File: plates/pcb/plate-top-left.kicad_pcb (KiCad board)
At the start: 2 copper layers, 125.1 x 92.6 mm, 0 parts

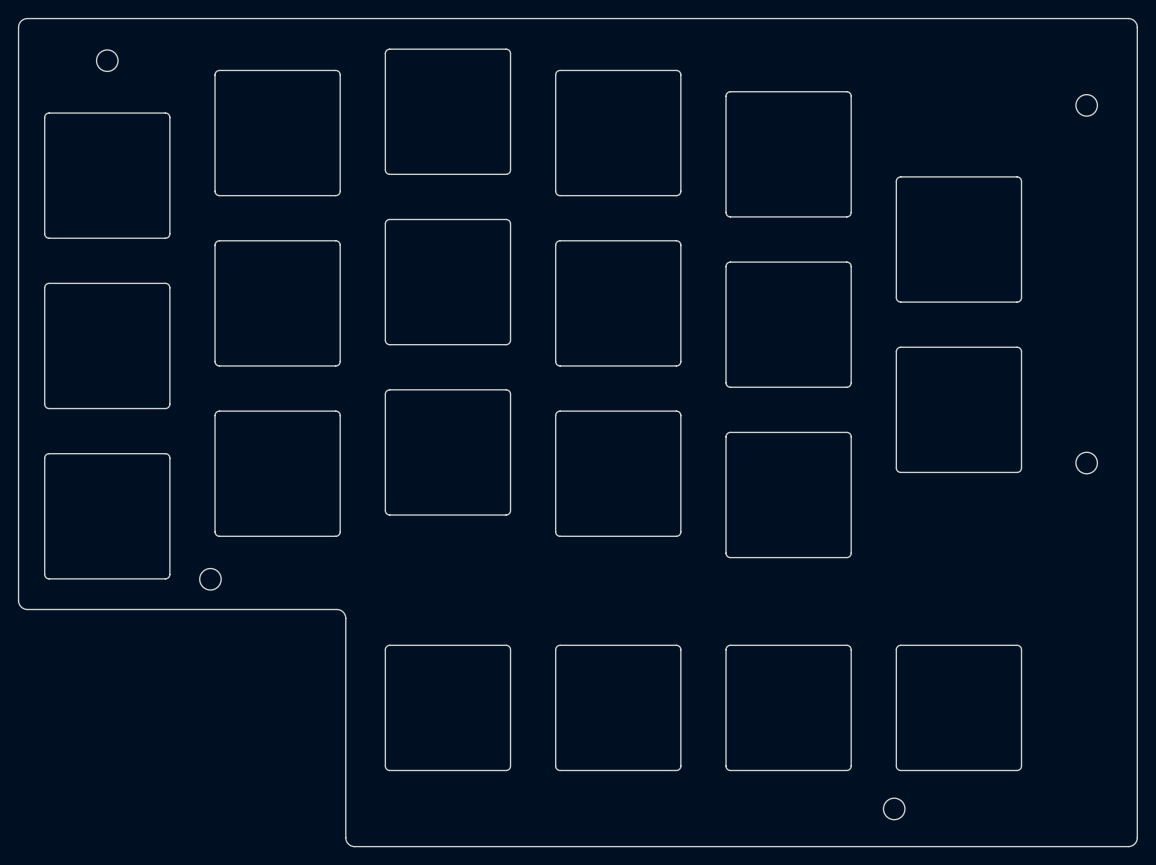
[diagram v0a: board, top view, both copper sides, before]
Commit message: fix(cad): update Z-stackup, 6mm cup standoffs, cup ear/plate clearances, ceramic ball throat, and sensor/CKW12 models
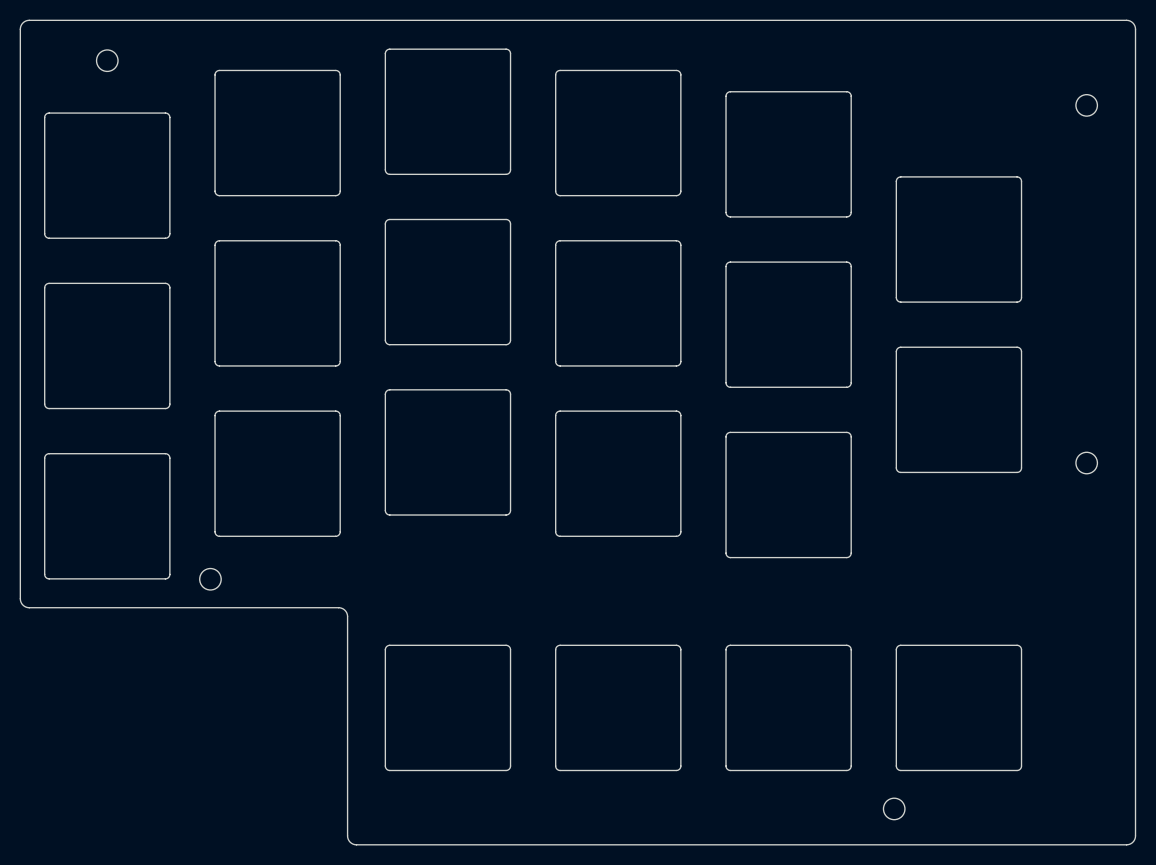
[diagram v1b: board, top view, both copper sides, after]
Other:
- board size 125.1 x 92.6 mm -> 124.7 x 92.2 mm
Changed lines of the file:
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@@
 	)
 	(gr_line
-		(start -119.4625 -23.7125)
-		(end -119.4625 40.38125)
-		(stroke
-			(width 0.15)
-			(type default)
-		)
-		(layer "Edge.Cuts")
-	)
-	(gr_arc
-		(start -119.4625 -23.7125)
-		(mid -119.169607 -24.419607)
-		(end -118.4625 -24.7125)
-		(stroke
-			(width 0.15)
-			(type default)
-		)
-		(layer "Edge.Cuts")
-	)
-	(gr_arc
-		(start -118.4625 41.38125)
-		(mid -119.169607 41.088357)
-		(end -119.4625 40.38125)
-		(stroke
-			(width 0.15)
-			(type default)
-		)
-		(layer "Edge.Cuts")
-	)
-	(gr_line
-		(start -118.4625 41.38125)
-		(end -83.8625 41.38125)
+		(start -119.2625 -23.5125)
+		(end -119.2625 40.18125)
+		(stroke
+			(width 0.15)
+			(type default)
+		)
+		(layer "Edge.Cuts")
+	)
+	(gr_arc
+		(start -119.2625 -23.5125)
+		(mid -118.969607 -24.219607)
+		(end -118.2625 -24.5125)
+		(stroke
+			(width 0.15)
+			(type default)
+		)
+		(layer "Edge.Cuts")
+	)
+	(gr_arc
+		(start -118.2625 41.18125)
+		(mid -118.969607 40.888357)
+		(end -119.2625 40.18125)
+		(stroke
+			(width 0.15)
+			(type default)
+		)
+		(layer "Edge.Cuts")
+	)
+	(gr_line
+		(start -118.2625 41.18125)
+		(end -83.6625 41.18125)
 		(stroke
 			(width 0.15)
@@
 	)
 	(gr_arc
-		(start -83.8625 41.38125)
-		(mid -83.155393 41.674143)
-		(end -82.8625 42.38125)
+		(start -83.6625 41.18125)
+		(mid -82.955393 41.474143)
+		(end -82.6625 42.18125)
 		(stroke
 			(width 0.15)
@@
 	)
 	(gr_line
-		(start -82.8625 42.38125)
-		(end -82.8625 66.9)
-		(stroke
-			(width 0.15)
-			(type default)
-		)
-		(layer "Edge.Cuts")
-	)
-	(gr_arc
-		(start -81.8625 67.9)
-		(mid -82.569607 67.607107)
-		(end -82.8625 66.9)
-		(stroke
-			(width 0.15)
-			(type default)
-		)
-		(layer "Edge.Cuts")
-	)
-	(gr_line
-		(start -81.8625 67.9)
-		(end 4.6625 67.9)
+		(start -82.6625 42.18125)
+		(end -82.6625 66.7)
+		(stroke
+			(width 0.15)
+			(type default)
+		)
+		(layer "Edge.Cuts")
+	)
+	(gr_arc
+		(start -81.6625 67.7)
+		(mid -82.369607 67.407107)
+		(end -82.6625 66.7)
+		(stroke
+			(width 0.15)
+			(type default)
+		)
+		(layer "Edge.Cuts")
+	)
+	(gr_line
+		(start -81.6625 67.7)
+		(end 4.4625 67.7)
 		(stroke
 			(width 0.15)
@@
 	)
 	(gr_line
-		(start 4.6625 -24.7125)
-		(end -118.4625 -24.7125)
-		(stroke
-			(width 0.15)
-			(type default)
-		)
-		(layer "Edge.Cuts")
-	)
-	(gr_arc
-		(start 4.6625 -24.7125)
-		(mid 5.369607 -24.419607)
-		(end 5.6625 -23.7125)
-		(stroke
-			(width 0.15)
-			(type default)
-		)
-		(layer "Edge.Cuts")
-	)
-	(gr_arc
-		(start 5.6625 66.9)
-		(mid 5.369607 67.607107)
-		(end 4.6625 67.9)
-		(stroke
-			(width 0.15)
-			(type default)
-		)
-		(layer "Edge.Cuts")
-	)
-	(gr_line
-		(start 5.6625 66.9)
-		(end 5.6625 -23.7125)
-		(stroke
-			(width 0.15)
+		(start 4.4625 -24.5125)
+		(end -118.2625 -24.5125)
+		(stroke
+			(width 0.15)
+			(type default)
+		)
+		(layer "Edge.Cuts")
+	)
+	(gr_arc
+		(start 4.4625 -24.5125)
+		(mid 5.169607 -24.219607)
+		(end 5.4625 -23.5125)
+		(stroke
+			(width 0.15)
+			(type default)
+		)
+		(layer "Edge.Cuts")
+	)
+	(gr_arc
+		(start 5.4625 66.7)
+		(mid 5.169607 67.407107)
+		(end 4.4625 67.7)
+		(stroke
+			(width 0.15)
+			(type default)
+		)
+		(layer "Edge.Cuts")
+	)
+	(gr_line
+		(start 5.4625 66.7)
+		(end 5.4625 -23.5125)
+		(stroke
+			(width 0.15)

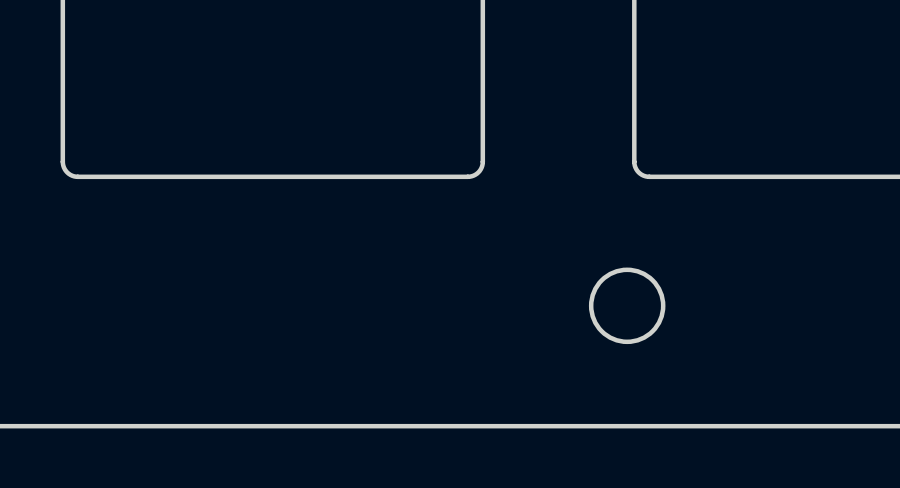
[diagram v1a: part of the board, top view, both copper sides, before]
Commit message: feat(pcb): separate pmw3360 sensor PCB with JST SH 6-pin connector and add symmetric thumb mounting holes L5/R5
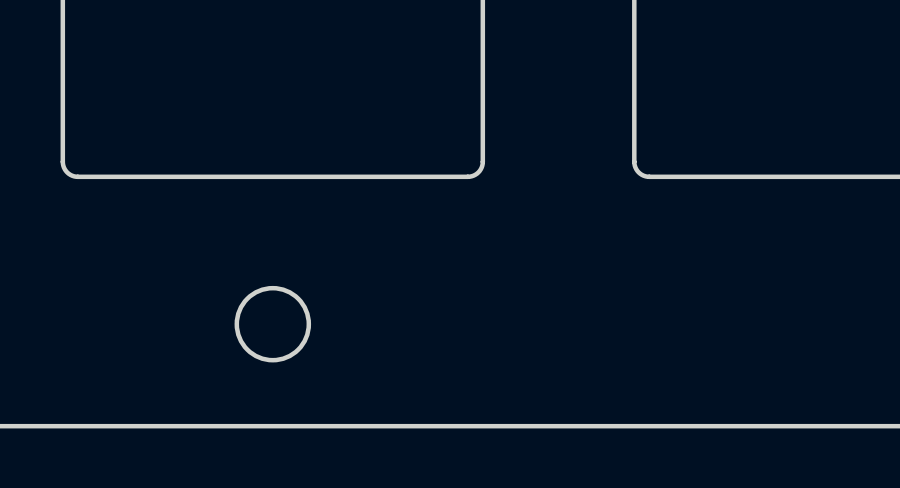
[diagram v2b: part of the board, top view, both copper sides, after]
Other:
- outline, holes or cut-outs redrawn
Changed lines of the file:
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@@
+		(layer "Edge.Cuts")
+	)
+	(gr_circle
+		(center -33.3375 64.3)
+		(end -32.137499 64.3)
+		(stroke
+			(width 0.15)
+			(type default)
+		)
+		(fill no)
 		(layer "Edge.Cuts")
 	)
@@
 		(layer "Edge.Cuts")
 	)
-	(gr_circle
-		(center -21.525 63.6875)
-		(end -20.325 63.6875)
-		(stroke
-			(width 0.15)
-			(type default)
-		)
-		(fill no)
-		(layer "Edge.Cuts")
-	)

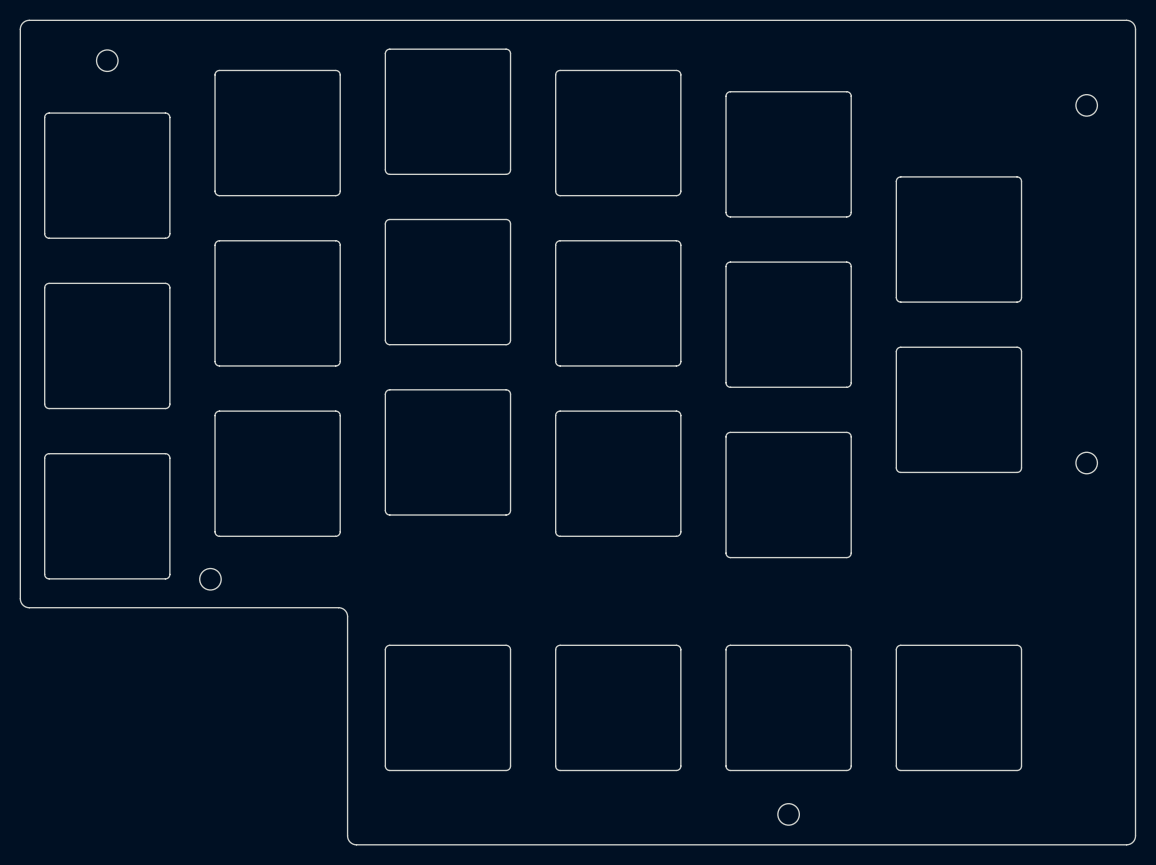
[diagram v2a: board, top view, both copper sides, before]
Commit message: feat(pcb,plates): face-to-face JST SH orientation, move TRRS jack north, and refine mounting holes
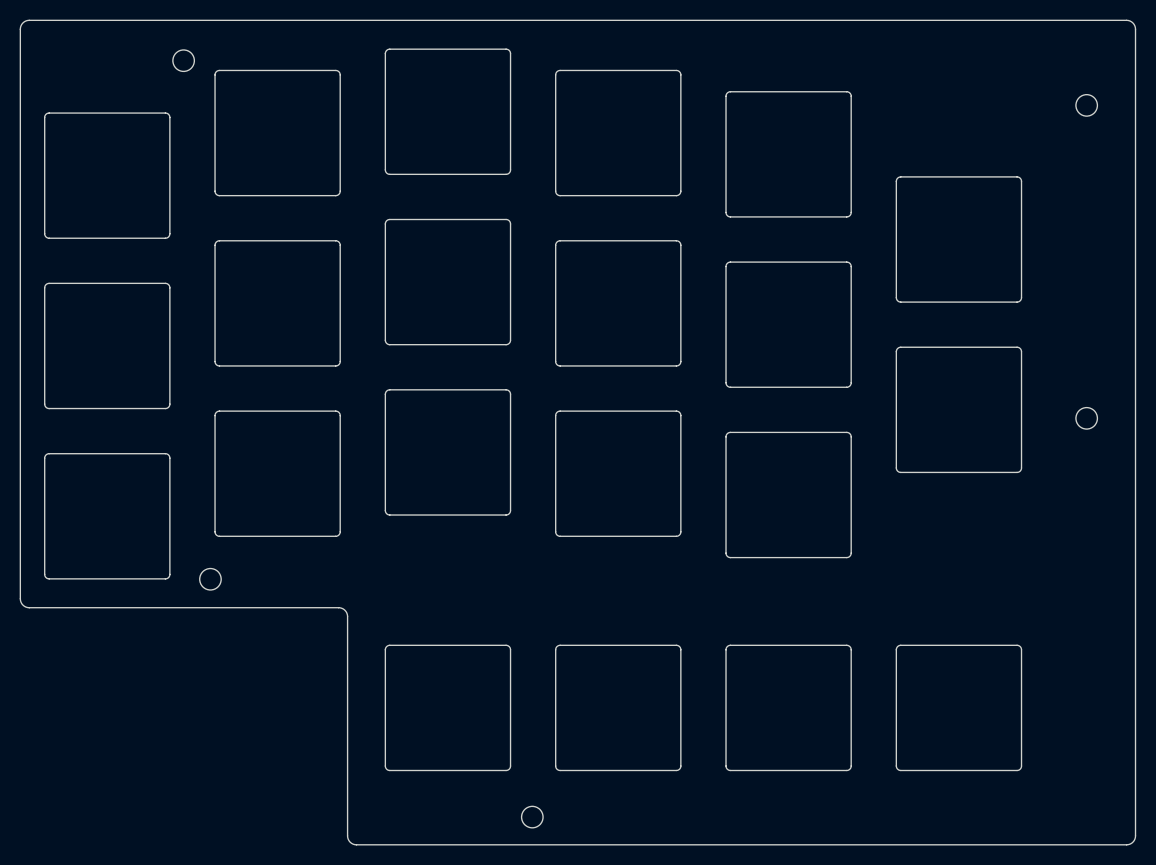
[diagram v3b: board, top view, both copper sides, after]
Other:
- outline, holes or cut-outs redrawn
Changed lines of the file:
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@@
-		(layer "Edge.Cuts")
-	)
-	(gr_circle
-		(center -109.5375 -20)
-		(end -108.337499 -20)
-		(stroke
-			(width 0.15)
-			(type default)
-		)
-		(fill no)
 		(layer "Edge.Cuts")
 	)
@@
 	)
 	(gr_circle
+		(center -101 -20)
+		(end -99.8 -20)
+		(stroke
+			(width 0.15)
+			(type default)
+		)
+		(fill no)
+		(layer "Edge.Cuts")
+	)
+	(gr_circle
 		(center -98 38)
 		(end -96.8 38)
@@
 		(layer "Edge.Cuts")
 	)
+	(gr_circle
+		(center -62 64.599999)
+		(end -60.8 64.599999)
+		(stroke
+			(width 0.15)
+			(type default)
+		)
+		(fill no)
+		(layer "Edge.Cuts")
+	)
 	(gr_arc
 		(start -59.3875 -18.40625)
@@
 		(layer "Edge.Cuts")
 	)
-	(gr_circle
-		(center -33.3375 64.3)
-		(end -32.137499 64.3)
-		(stroke
-			(width 0.15)
-			(type default)
-		)
-		(fill no)
-		(layer "Edge.Cuts")
-	)
 	(gr_arc
 		(start -26.8375 -16.524999)
@@
 	)
 	(gr_circle
-		(center 0 25)
-		(end 1.2 25)
-		(stroke
-			(width 0.15)
+		(center 0 20)
+		(end 1.2 20)
+		(stroke
+			(width 0.15)
